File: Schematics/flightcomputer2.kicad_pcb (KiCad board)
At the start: 4 copper layers, 80 x 80 mm, 105 parts, among them J1 Microsemi_FlashPro-JTAG-10, J10 Pyro, J2 Pyro, J4 Drouge, J5 Conn_01x05_Pin, J6 Conn_01x05_Pin, J7 Conn_Coaxial_Small, J8 Micro_SD_Card, J9 USB_C_Receptacle_USB2.0_16P, Q1 IRLML2502TRPBF, Q2 IRLML2502TRPBF, Q3 BC817, Q4 IRLML2502TRPBF, Q6 Q_PMOS_GSD, SW1 SAMZO G4R0015010, SW2 SAMZO G4R0015010, U1 STM32F405RGT6, U2 SN65HVD230, U3 PowerIn, U4 LDL1117-3.3, U5 RFM95W-915S2, U6 Bosch BMP388, U7 LSM6DS3TR-C, U8 W25Q128JVP, U9 H3LIS331DL, Y1 8mhz

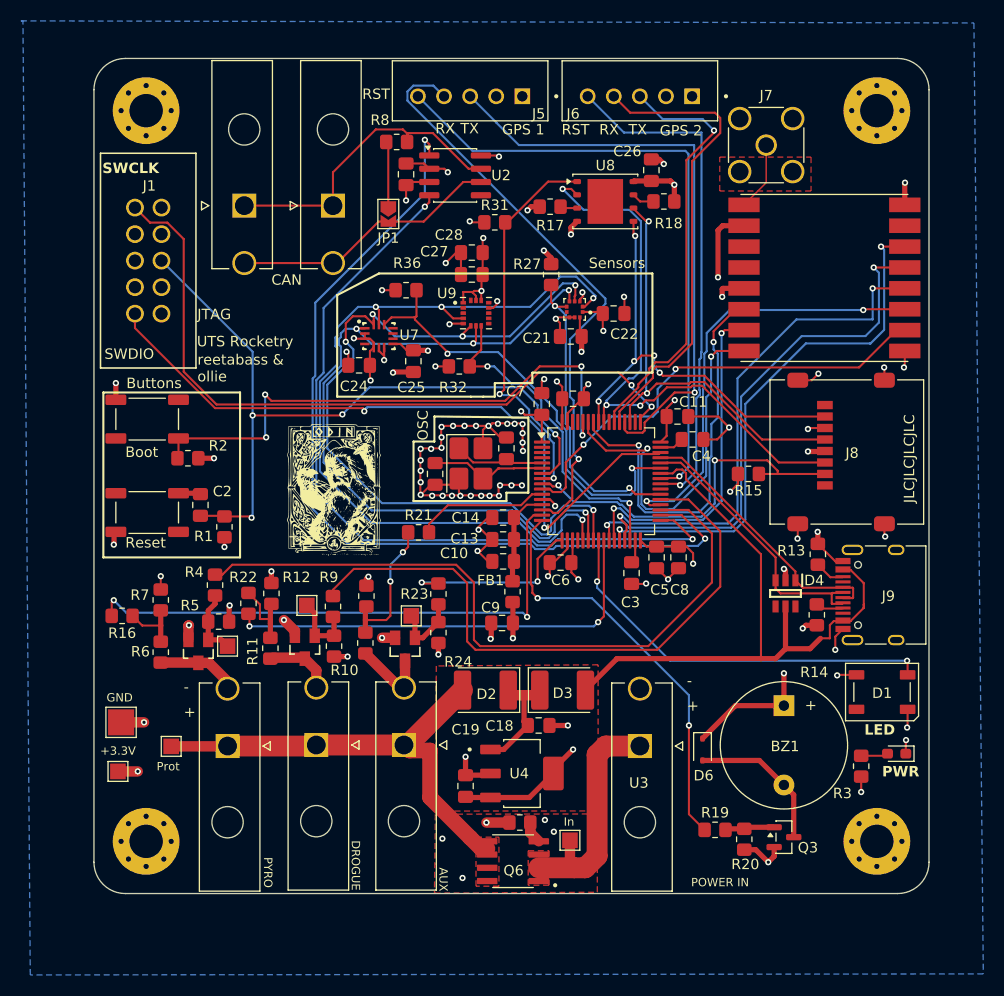
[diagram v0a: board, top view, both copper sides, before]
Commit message: ran drc no warnings/errors
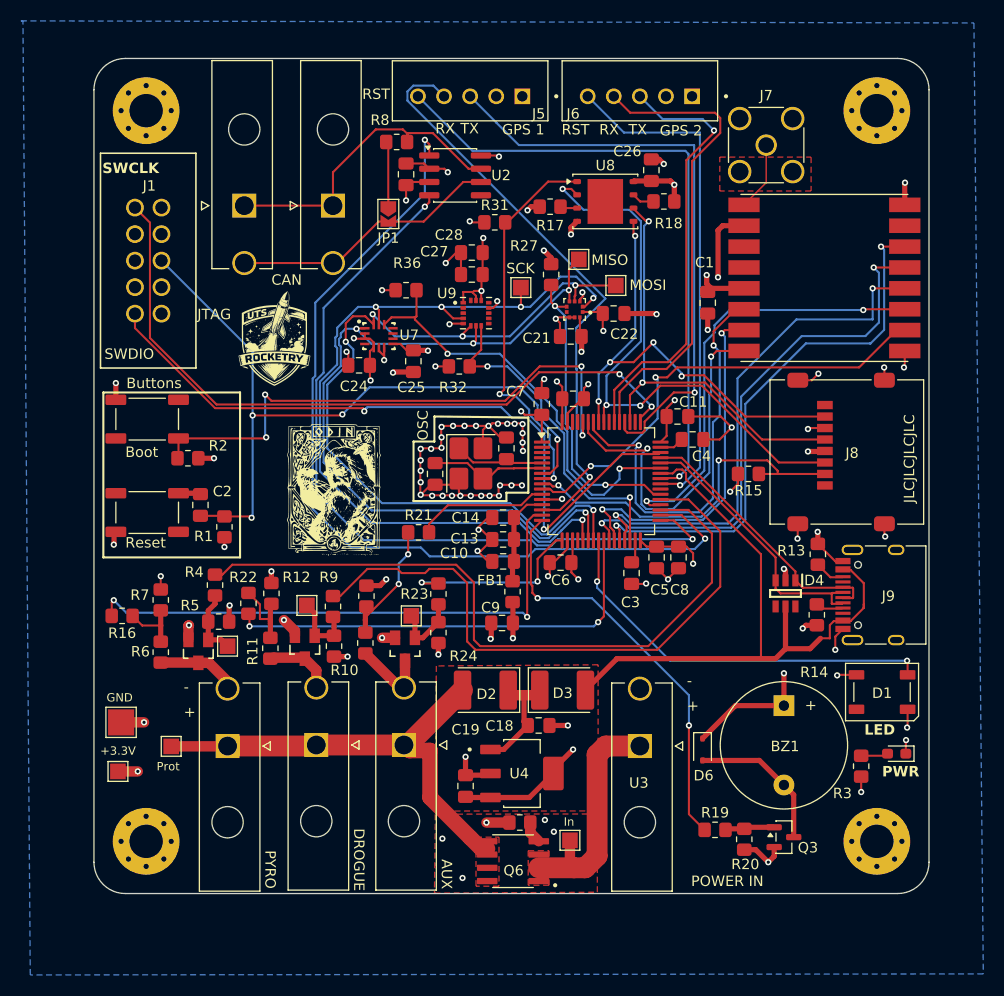
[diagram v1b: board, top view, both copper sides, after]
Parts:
- added C1: 100nf, Capacitor_SMD:C_0805_2012Metric_Pad1.18x1.45mm_HandSolder, F.Cu at (173.8, 71.4)
- added G***: LOGO, LOGO, F.Cu at (132.3, 75.3)
- added TP10: TestPoint, TestPoint:TestPoint_Pad_1.5x1.5mm, F.Cu at (155.9, 70.0)
- added TP8: TestPoint, TestPoint:TestPoint_Pad_1.5x1.5mm, F.Cu at (161.4, 67.2)
- added TP9: TestPoint, TestPoint:TestPoint_Pad_1.5x1.5mm, F.Cu at (165.0, 69.8)
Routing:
- net GND: track 156.1 -> 161.2 mm, vias 88 -> 89
- net /Accelerometer/Accelerometer_MOSI: track 76.9 -> 80.2 mm
- net /FlashMemory/SPI_MOSI: track 42.3 -> 45.5 mm
- net /Accelerometer/Accelerometer_MIS0: track 74.3 -> 77.0 mm
- net +3.3V: track 107.9 -> 109.6 mm
- net /LoRa/sxDIO1: track 32.9 -> 34.6 mm
- net /IMU/ChipSelectIMU: track 42.3 -> 41.1 mm
- net Net-(R21-Pad1): track 13.7 -> 12.5 mm
- net /MCU/SWCLK: track 69.0 -> 68.0 mm
- net /Accelerometer/Accelerometer_SPICLK: track 79.9 -> 81.0 mm, vias 4 -> 5
- net /LoRa/sxNSS: track 51.3 -> 52.3 mm
- net /LoRa/sxReset: track 51.4 -> 52.3 mm
- net /GPS/GPS2_TX: track 41.0 -> 41.8 mm
- net /LoRa/sxSCK: track 48.9 -> 49.6 mm
- net /GPS/GPS2_RX: track 44.9 -> 45.5 mm
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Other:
- board text added: "MISO"
- board text added: "MOSI"
- board text added: "SCK"
- board text removed: "Sensors"
- board text removed: "UTS Rocketry"
- board text removed: "reetabass & ollie"

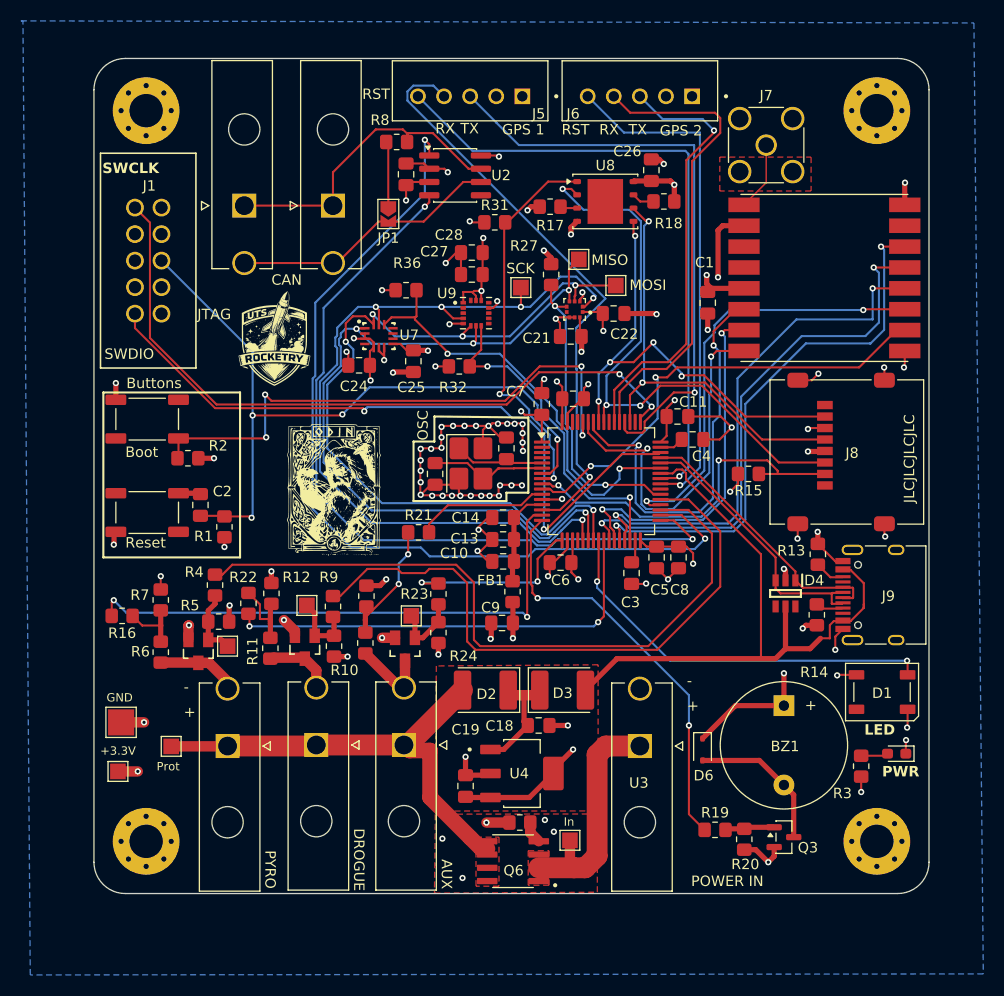
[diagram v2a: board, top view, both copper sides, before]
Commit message: updated to KiCad 10.0, updated .gitignore
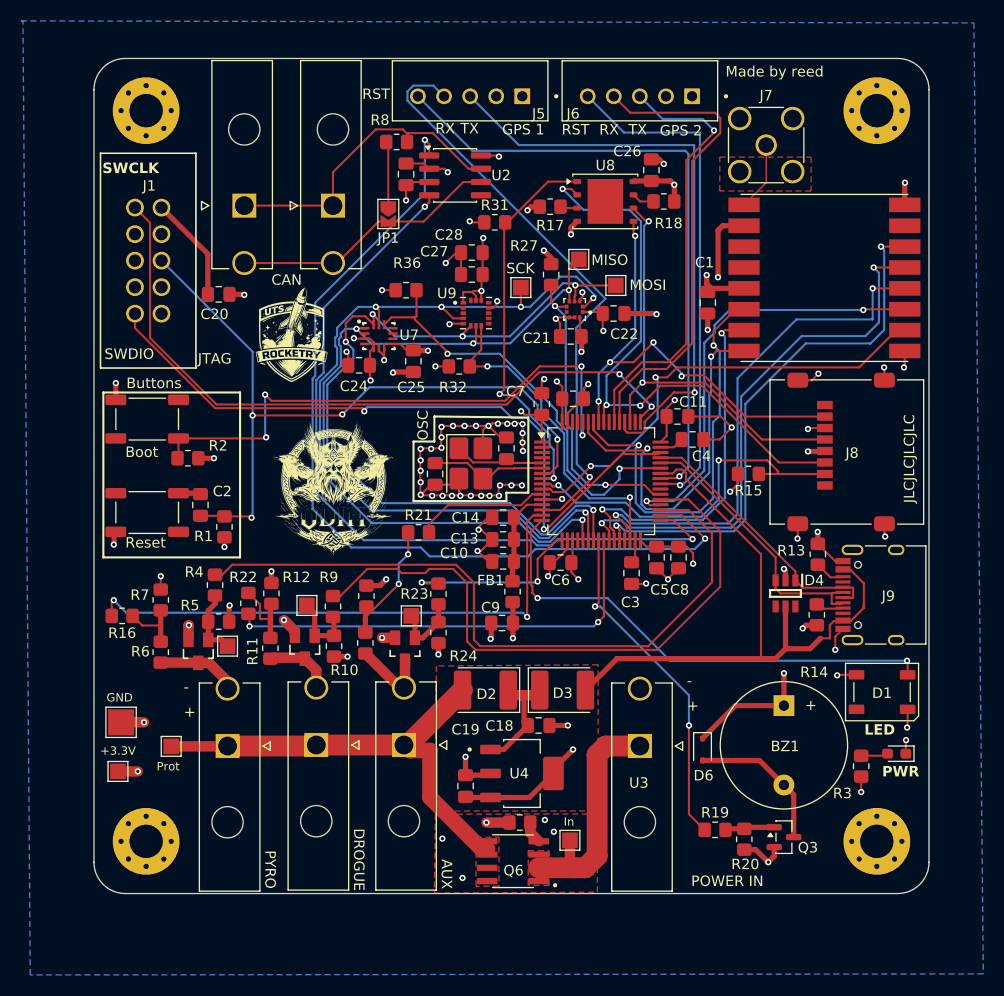
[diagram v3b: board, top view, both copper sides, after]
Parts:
- added C20: 100nf, Capacitor_SMD:C_0805_2012Metric_Pad1.18x1.45mm_HandSolder, F.Cu at (127.0, 70.6)
- moved G*** 1.69 mm to (133.9, 74.9)
- moved G*** 0.11 mm to (137.9, 89.3)
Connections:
- U1 pad 16: /MCU/BuzzerControl -> /MCU/RGB_DATA
- U1 pad 24: /MCU/RGB_DATA -> /MCU/BuzzerControl
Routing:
- net +3.3V: track 109.6 -> 119.8 mm
- net /MCU/RGB_DATA: track 38.6 -> 47.4 mm
- net /MCU/BuzzerControl: track 40.0 -> 32.5 mm
- net GND: track 161.2 -> 162.6 mm, vias 89 -> 90
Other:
- board text added: "Made by reed"

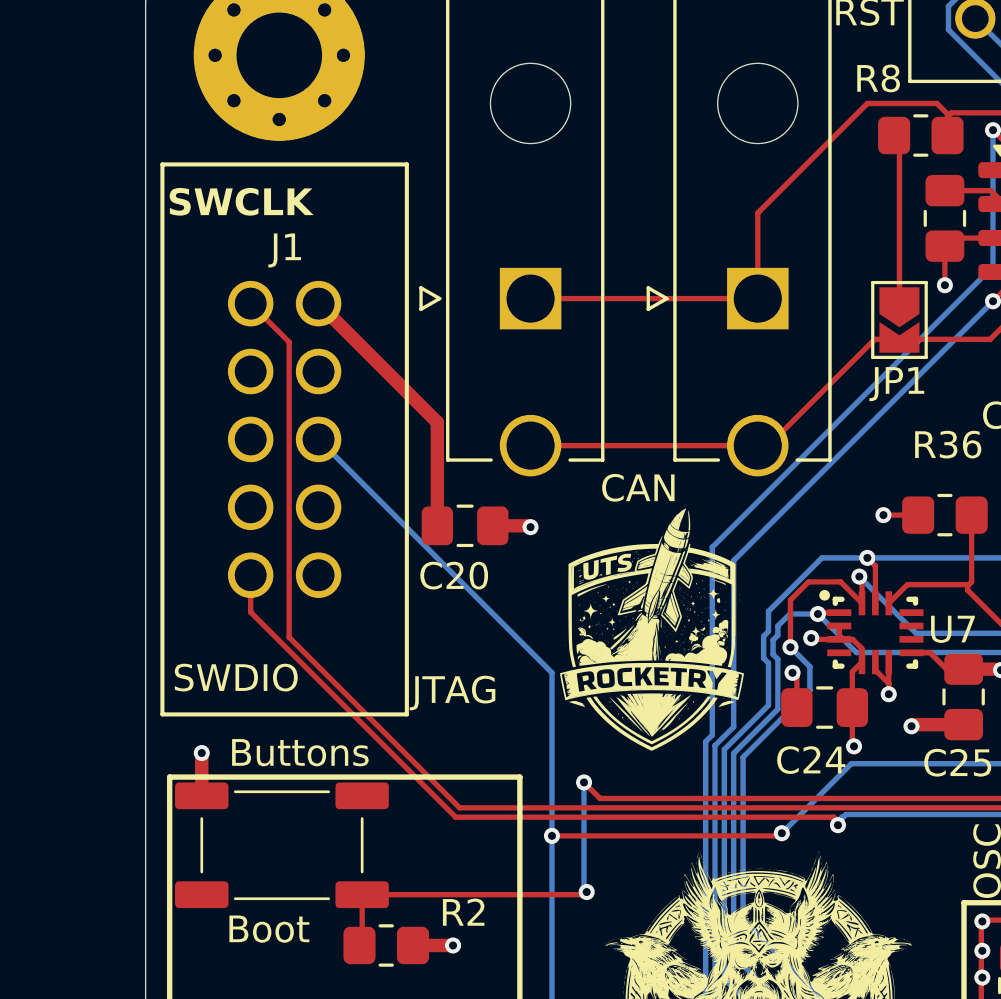
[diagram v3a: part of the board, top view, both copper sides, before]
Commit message: updated stlink
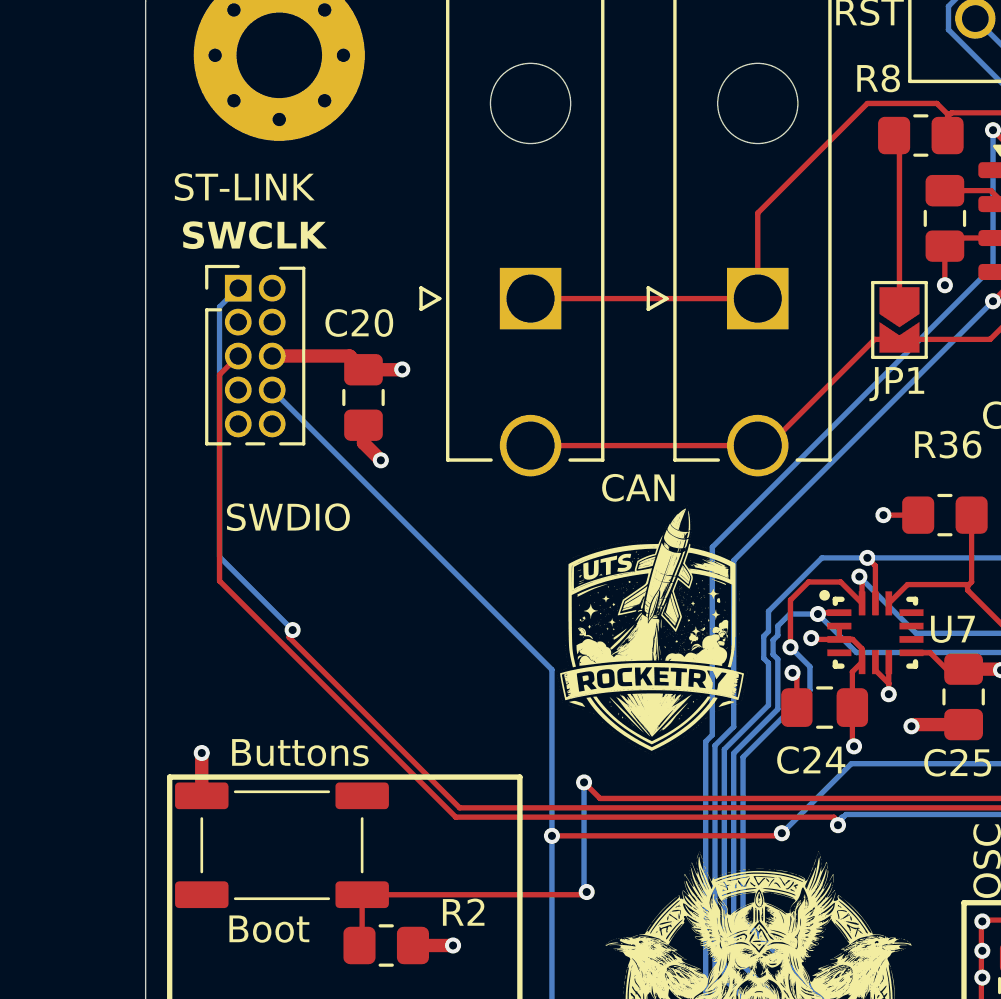
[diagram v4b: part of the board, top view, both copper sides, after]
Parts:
- J1: footprint myFootprints:CONN_7024610XX_MOL -> Connector_PinHeader_1.27mm:PinHeader_2x05_P1.27mm_Vertical
- moved C20 6.12 mm to (123.2, 65.8), turned to -90 degrees
- moved J1 0.74 mm to (118.5, 61.7), turned to 0 degrees
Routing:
- net /MCU/SWDIO: track 68.6 -> 77.6 mm
- net +3.3V: track 119.8 -> 114.7 mm, vias 30 -> 31
- net /MCU/NRST: track 70.7 -> 73.3 mm
- net /MCU/SWCLK: track 68.0 -> 69.4 mm, vias 2 -> 3
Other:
- board text added: "ST-LINK"
- board text removed: "JTAG"
